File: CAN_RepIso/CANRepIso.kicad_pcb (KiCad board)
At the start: 4 copper layers, 57 x 27 mm, 82 parts, among them U1 SN74LV32ADGVR, U10 AP2205-33W5-7, U11 AP2205-33W5-7, U2 SN74LVC2G08DCUR, U3 SN74LVC2G07DBVR, U4 SN74LVC2G04DBVR, U5 SN74LVC2G132DCUR, U6 SN65HVD230, U7 PLACEHOLDER ISOLATOR, U8 SN65HVD230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

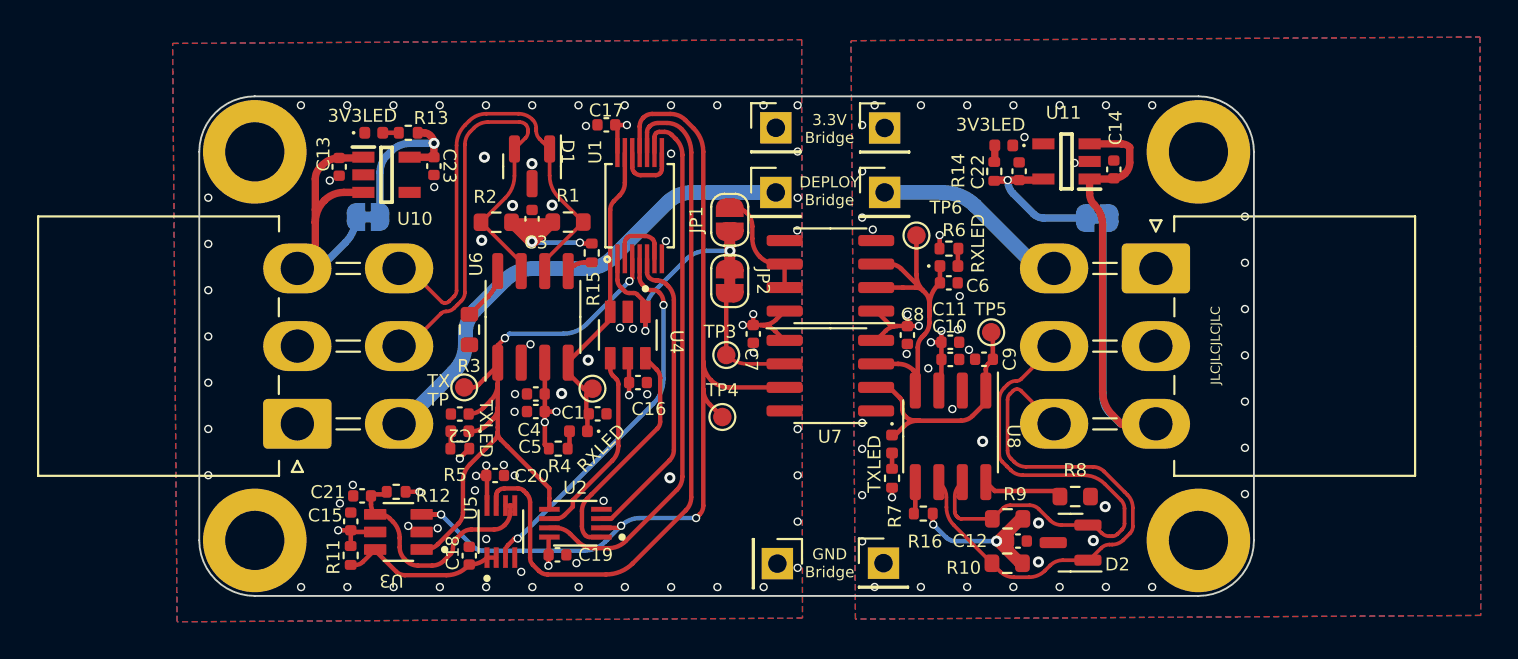
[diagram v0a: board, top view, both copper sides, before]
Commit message: silkscreen tweaks
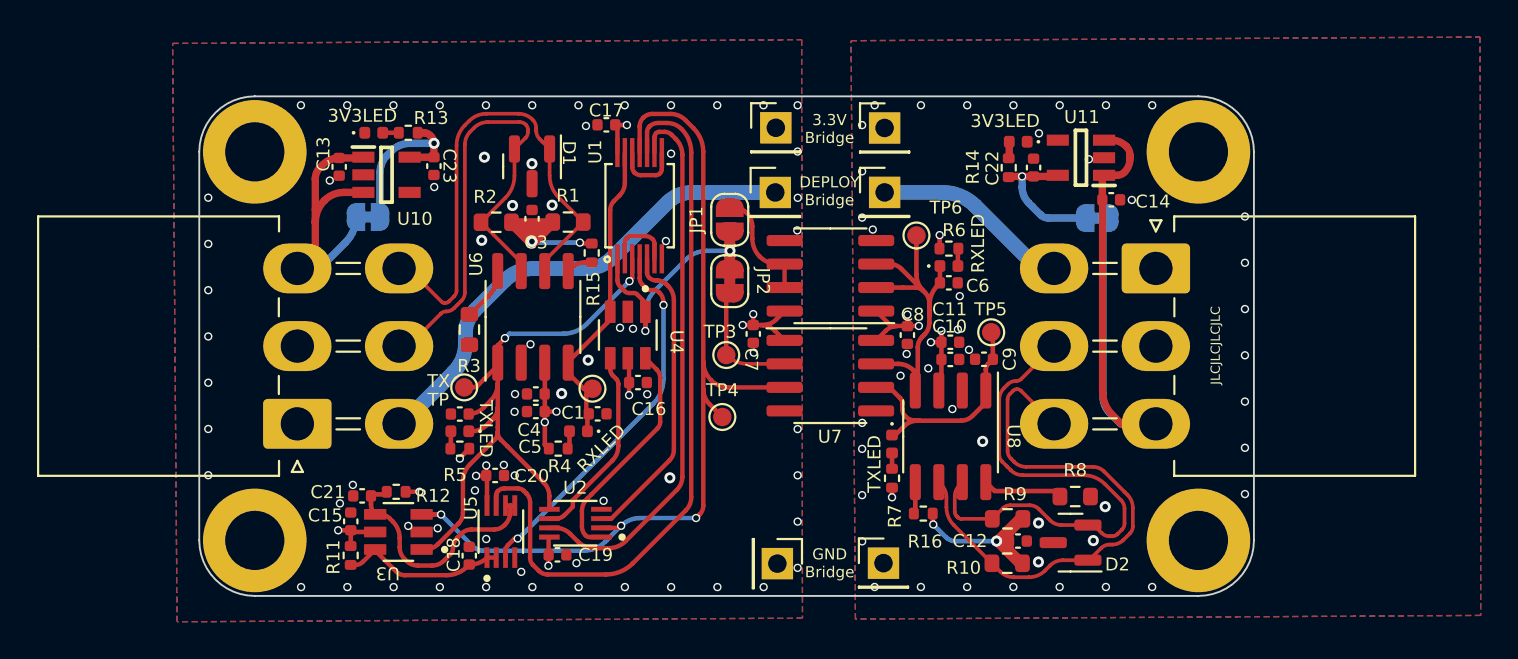
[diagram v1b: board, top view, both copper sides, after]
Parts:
- moved C14 1.65 mm to (161.3, 88.6), turned to 0 degrees
- moved C22 0.81 mm to (157.1, 86.8)
- moved D8 0.81 mm to (156.3, 85.5)
- moved R14 0.81 mm to (155.7, 86.9)
- moved U11 0.81 mm to (159.7, 86.3)
- moved G*** 0.11 mm to (146.6, 97.4)
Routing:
- net /RBUS_uC_V2: track 34.8 -> 33.1 mm
- net GND1: vias 42 -> 44

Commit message: some DRC
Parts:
- moved R15 1.01 mm to (133.2, 92.5), turned to -90 degrees
- moved TP6 0.81 mm to (151.0, 91.3)
- moved R8 0.65 mm to (158.7, 104.6)
- moved R6 0.46 mm to (153.0, 91.1)
- moved D5 0.44 mm to (153.0, 92.1)
- moved C6 0.43 mm to (152.9, 93.1)
- moved TP5 0.17 mm to (154.8, 95.6)
- moved C11 0.10 mm to (152.6, 96.2)
- moved R7 0.09 mm to (149.4, 103.7)
- moved R1 0.07 mm to (132.0, 89.8)
- moved R2 0.07 mm to (128.0, 89.8)
- moved C9 0.07 mm to (154.5, 97.2)
- moved D6 0.07 mm to (149.4, 101.8)
- moved C10 0.06 mm to (152.6, 97.2)
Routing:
- net /Vref: track 9.40 -> 12.9 mm, vias 2 -> 1
- net /RX2_PRE_ISO: track 20.1 -> 18.9 mm
- net Net-(U8-Rs): track 4.33 -> 3.68 mm
- net +3.3VA: track 17.4 -> 16.8 mm, vias 7 -> 6

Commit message: oops forgot a connection
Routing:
- net /RX2_PRE_ISO: track 18.9 -> 20.3 mm
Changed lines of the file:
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@@
   (segment (start 150.7 97.91) (end 150.7 98.9) (width 0.25) (layer "F.Cu") (net 6))
   (segment (start 151.115 93.495) (end 151.212512 93.592512) (width 0.25) (layer "F.Cu") (net 6))
+  (segment (start 150.76 91.502) (end 150.953 91.309) (width 0.25) (layer "F.Cu") (net 6))
   (segment (start 152.458 93.079) (end 152.458 92.116142) (width 0.25) (layer "F.Cu") (net 6))
+  (segment (start 150.76 92.637955) (end 150.76 91.502) (width 0.25) (layer "F.Cu") (net 6))
   (segment (start 148.585 92.065) (end 149.321548 92.065) (width 0.25) (layer "F.Cu") (net 6))
   (segment (start 150.5885 97.7985) (end 150.7 97.91) (width 0.25) (layer "F.Cu") (net 6))
@@
   (arc (start 152.36 106.83) (mid 152.592606 106.985423) (end 152.866984 107.04) (width 0.25) (layer "B.Cu") (net 20))
   (segment (start 153.451 92.0105) (end 153.451 91.0955) (width 0.25) (layer "F.Cu") (net 21))
-  (segment (start 153 91.255) (end 153.025 91.23) (width 0.25) (layer "F.Cu") (net 21))
   (segment (start 149.372 103.1925) (end 149.372 102.3375) (width 0.25) (layer "F.Cu") (net 22))
   (segment (start 122.785 84.97) (end 121.915 84.97) (width 0.25) (layer "F.Cu") (net 23))
